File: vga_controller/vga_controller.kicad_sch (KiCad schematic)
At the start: 51 parts

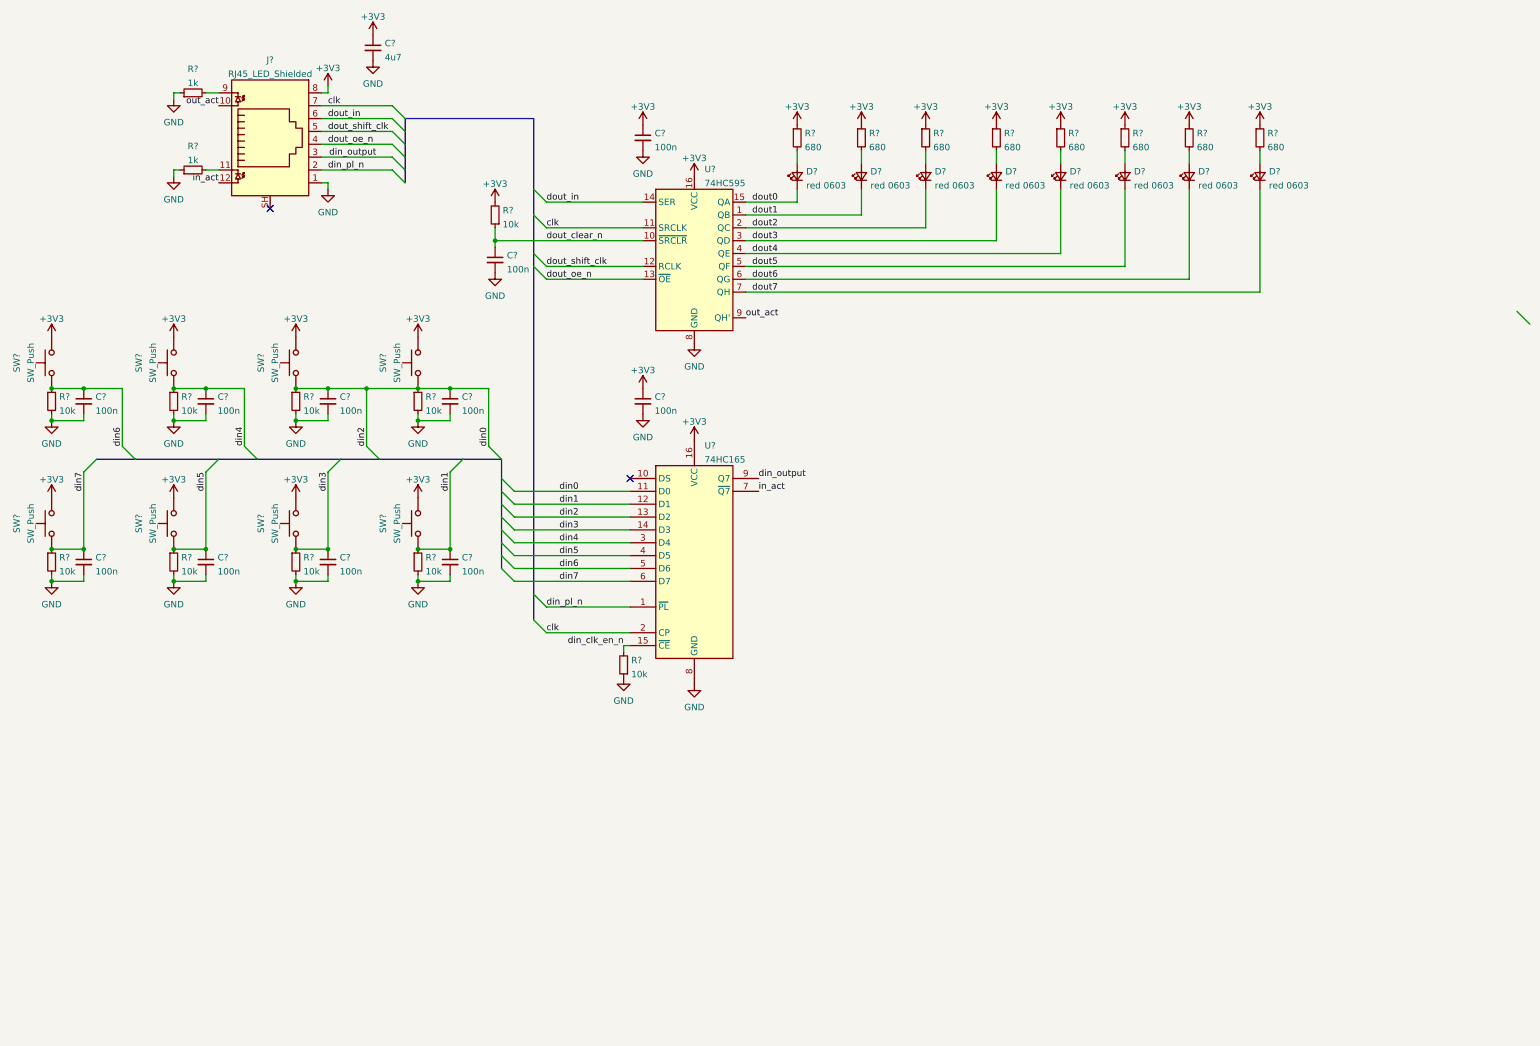
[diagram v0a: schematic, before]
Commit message: schema done, pcb routed
for controller
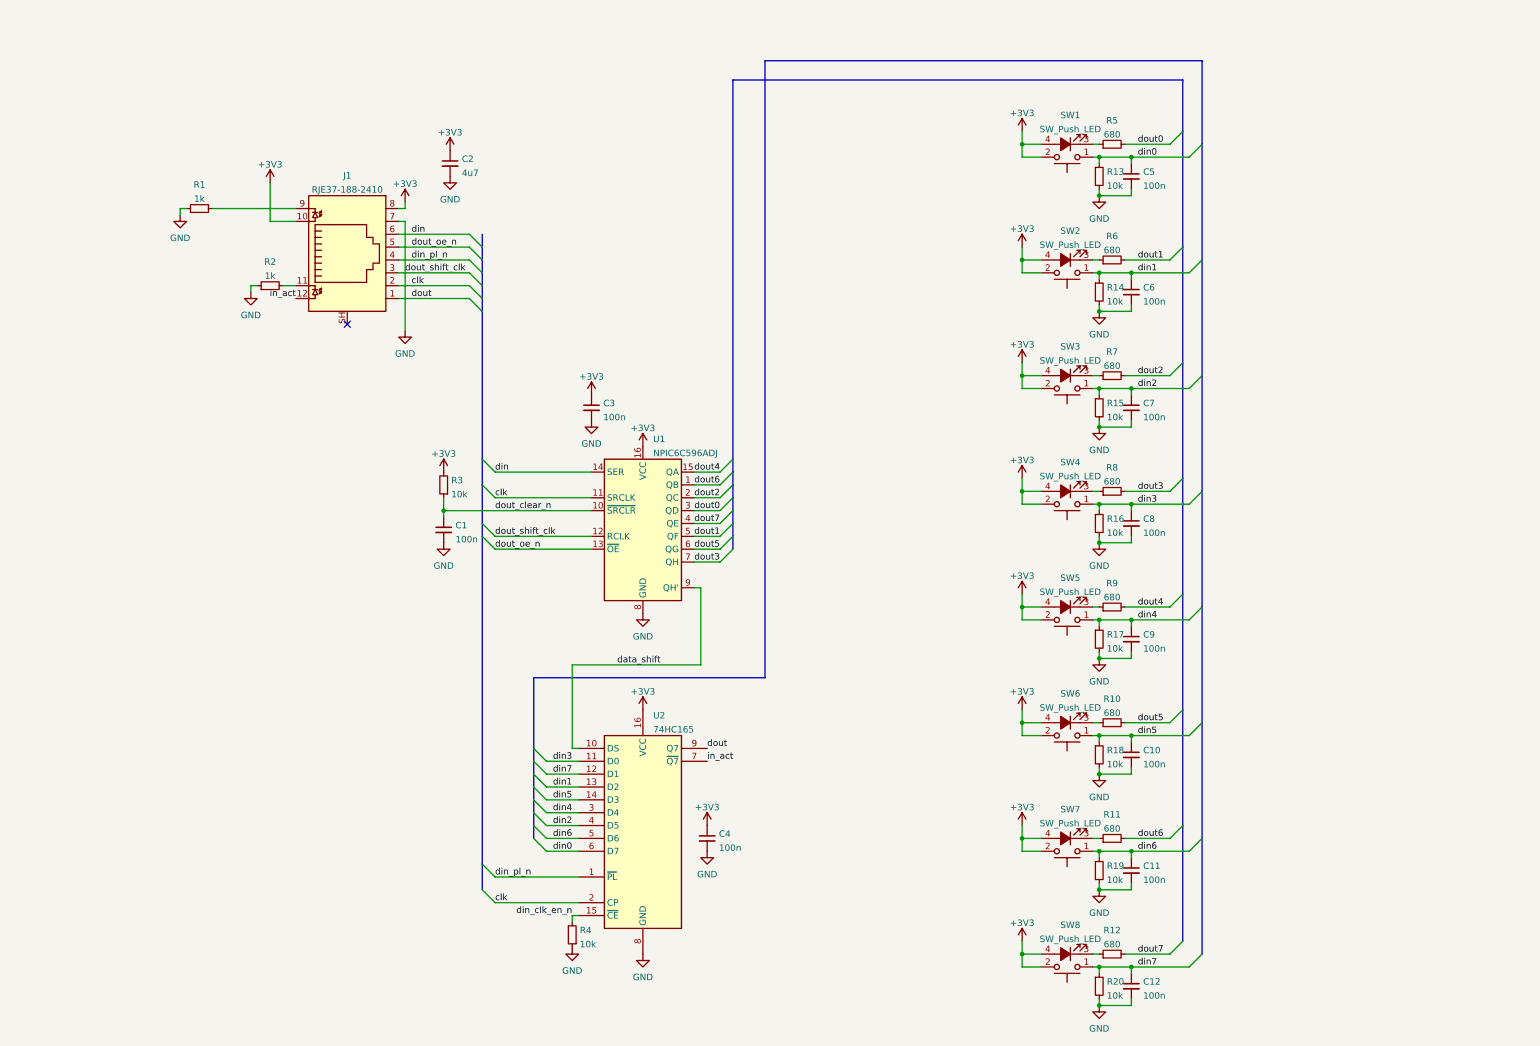
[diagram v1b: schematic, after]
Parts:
- removed C? (x8): 100n, symbol Device:C_Small
- removed D? (x8): red 0603, symbol Device:LED_Small
- removed R? (x8): 680, symbol Device:R_Small
- removed R? (x8): 10k, symbol Device:R_Small
- removed SW? (x8): SW_Push, symbol Switch:SW_Push
- added C10, C11, C12, C5, C6, C7, C8, C9: 100n, Capacitor_SMD:C_0603_1608Metric_Pad1.08x0.95mm_HandSolder, symbol Device:C_Small
- added R10, R11, R12, R5, R6, R7, R8, R9: 680, Resistor_SMD:R_0603_1608Metric_Pad0.98x0.95mm_HandSolder, symbol Device:R_Small
- added R13, R14, R15, R16, R17, R18, R19, R20: 10k, Resistor_SMD:R_0603_1608Metric_Pad0.98x0.95mm_HandSolder, symbol Device:R_Small
- added SW1, SW2, SW3, SW4, SW5, SW6, SW7, SW8: SW_Push_LED, good_things:SW_Cherry_MX_1.00u_PCB_smd_led, symbol Switch:SW_Push_LED
- C1, C2, C3, C4: renamed from C?; footprint (none) -> Capacitor_SMD:C_0603_1608Metric_Pad1.08x0.95mm_HandSolder
- J1: renamed from J?; value RJ45_LED_Shielded -> RJE37-188-2410; footprint (none) -> Connector_RJ:RJ45_Amphenol_RJHSE538X
- R1, R2, R3, R4: renamed from R?; footprint (none) -> Resistor_SMD:R_0603_1608Metric_Pad0.98x0.95mm_HandSolder
- U1: renamed from U?; value 74HC595 -> NPIC6C596ADJ; footprint (none) -> Package_SO:SOIC-16_3.9x9.9mm_P1.27mm
- U2: renamed from U?; footprint (none) -> Package_SO:SOIC-16_3.9x9.9mm_P1.27mm
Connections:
- net +3V3: now also J1.10, SW1.2, SW1.4 (A), SW2.2, SW2.4 (A), SW3.2, SW3.4 (A), SW4.2, SW4.4 (A), SW5.2, SW5.4 (A), SW6.2, SW6.4 (A), SW7.2, SW7.4 (A), SW8.2, SW8.4 (A)
- net GND: now also J1.3, J1.7, U1.12 (RCLK), C10.2, C11.2, C12.2, C5.2, C6.2, C7.2, C8.2, C9.2, R13.2, R14.2, R15.2, R16.2, R17.2, R18.2, R19.2, R20.2; no longer J1.1
- net clk: now also J1.2; no longer J1.7
- net din0: now also U2.6 (D7), C5.1, R13.1, SW1.1; no longer U2.11 (D0), U2.13 (D2)
- net din1: now also U2.13 (D2), C6.1, R14.1, SW2.1; no longer U2.12 (D1)
- net din3: now also U2.11 (D0), C8.1, R16.1, SW4.1; no longer U2.14 (D3)
- net din4: now also C9.1, R17.1, SW5.1
- net din5: now also U2.14 (D3), C10.1, R18.1, SW6.1; no longer U2.4 (D5)
- net din6: now also C11.1, R19.1, SW7.1
- net din7: now also U2.12 (D1), C12.1, R20.1, SW8.1; no longer U2.6 (D7)
- net din_pl_n: now also J1.4; no longer J1.2
- net dout0: now also U1.3 (QD), R5.2; no longer U1.15 (QA)
- net dout1: now also U1.5 (QF), R6.2; no longer U1.1 (QB)
- net dout2: now also R7.2
- net dout3: now also U1.7 (QH), R8.2; no longer U1.3 (QD)
- net dout4: now also U1.15 (QA), R9.2; no longer U1.4 (QE)
- net dout5: now also U1.6 (QG), R10.2; no longer U1.5 (QF)
- net dout6: now also U1.1 (QB), R11.2; no longer U1.6 (QG)
- net dout7: now also U1.4 (QE), R12.2; no longer U1.7 (QH)
- net dout_oe_n: now also J1.5; no longer J1.4
- net data_shift: now reaches U2.10 (DS)
- net data_shift: now also U1.9 (QH')
- net din_output renamed dout
- net dout: now also J1.1; no longer J1.3
- net dout_in renamed din
- removed net dout_shift_clk: J1.5, U1.12 (RCLK)
- removed net out_act: J1.10, U1.9 (QH')
- new net: R10.1, SW6.3 (K)
- new net: R8.1, SW4.3 (K)
- new net: R12.1, SW8.3 (K)
- new net: R9.1, SW5.3 (K)
- new net: R11.1, SW7.3 (K)
- new net: R7.1, SW3.3 (K)
- new net: R5.1, SW1.3 (K)
- new net: R6.1, SW2.3 (K)
- new net din2: C7.1, R15.1, SW3.1, U2.4 (D5)
- no-connect marks 2 -> 1
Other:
- moved on the sheet: C1, C2, C3, C4, J1, R1, R2, R3, R4, U1, U2

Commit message: Rev 4 of main board
controller rev1 done as well :D
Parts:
- added H1, H2, H3: MountingHole_Pad, MountingHole:MountingHole_3.2mm_M3_Pad, symbol Mechanical:MountingHole_Pad
- added R21: 10k, Resistor_SMD:R_0603_1608Metric_Pad0.98x0.95mm_HandSolder, symbol Device:R_Small
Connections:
- net GND: now also J1.5, H1.1, H2.1, H3.1, R21.1; no longer J1.3, U1.12 (RCLK)
- net din renamed copi
- net din_pl_n renamed ie_n
- net dout renamed cipo
- net dout_oe_n renamed oe_n
- net oe_n: now also R21.2; no longer J1.5
- new net out_shift_clk: J1.3, U1.12 (RCLK)
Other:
- moved on the sheet: C10, C11, C12, C5, C6, C7, C8, C9, R10, R11, R12, R13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

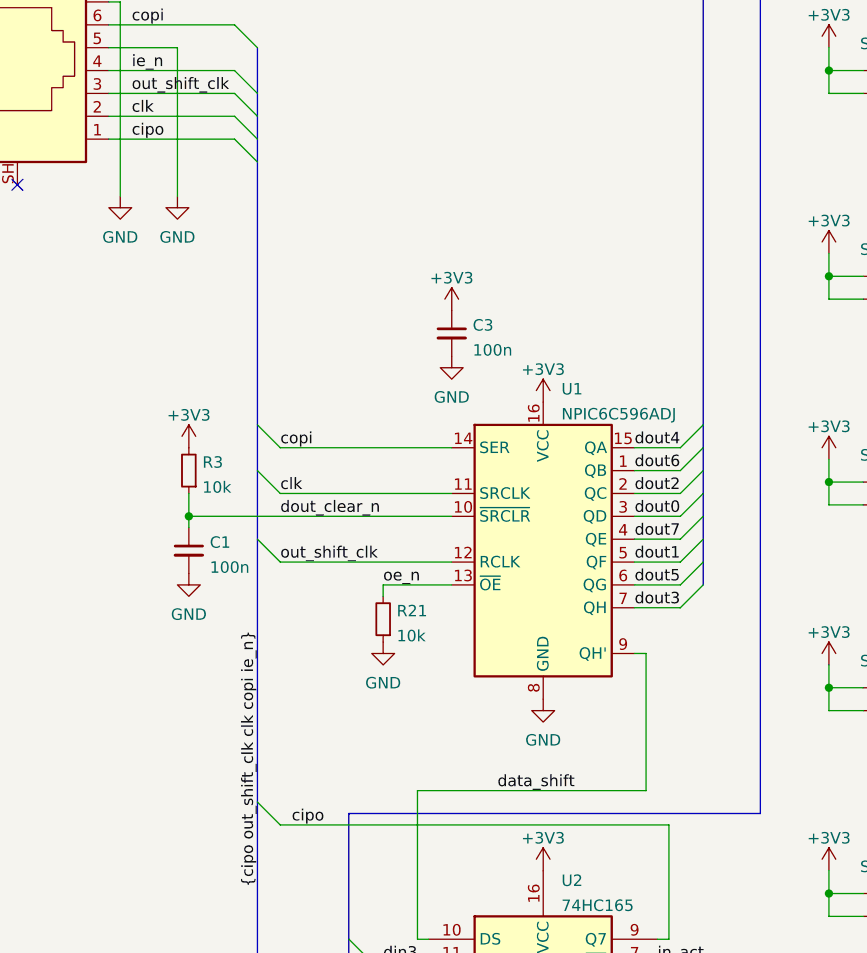
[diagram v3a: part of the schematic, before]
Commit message: fix issue with controller board
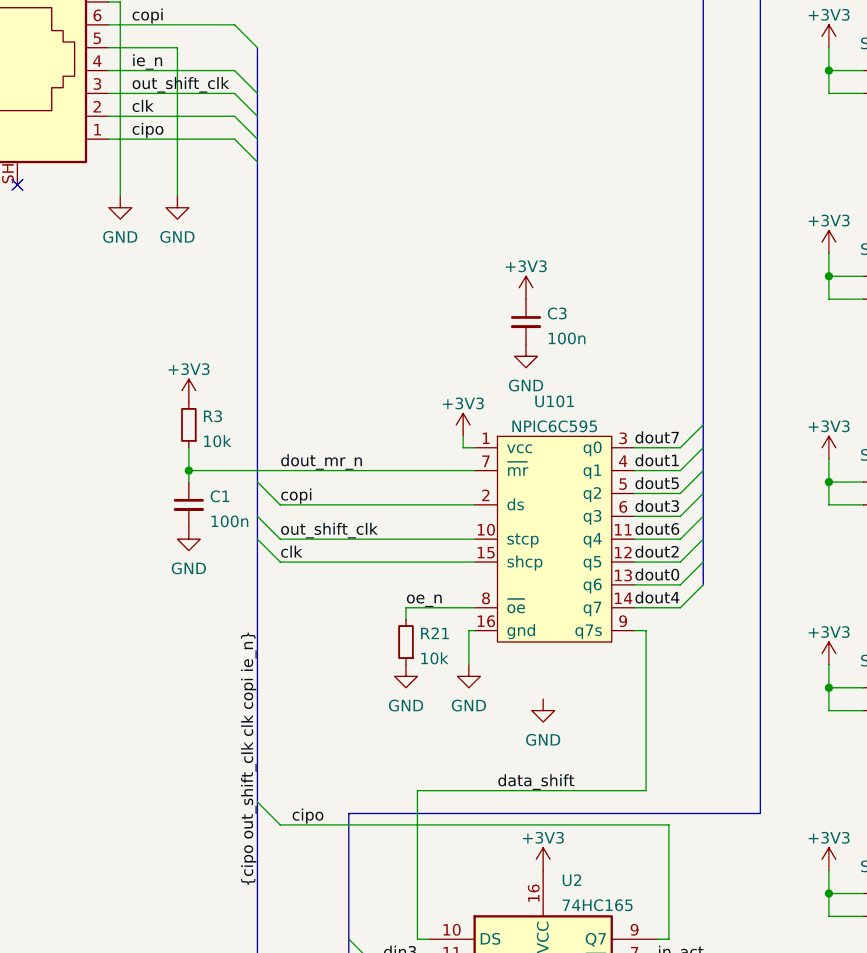
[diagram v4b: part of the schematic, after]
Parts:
- removed U1: NPIC6C596ADJ, Package_SO:SOIC-16_3.9x9.9mm_P1.27mm, symbol 74xx:74HC595
- added U101: NPIC6C595, Package_SO:SOIC-16_3.9x9.9mm_P1.27mm, symbol good_things:NPIC6C595
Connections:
- net +3V3: now also U101.1 (vcc)
- net GND: now also U101.16 (gnd)
- net clk: now also U101.15 (shcp)
- net copi: now also U101.2 (ds)
- net data_shift: now also U101.9 (q7s)
- net dout0: now also U101.13 (q6)
- net dout1: now also U101.4 (q1)
- net dout2: now also U101.12 (q5)
- net dout3: now also U101.6 (q3)
- net dout4: now also U101.14 (q7)
- net dout5: now also U101.5 (q2)
- net dout6: now also U101.11 (q4)
- net dout7: now also U101.3 (q0)
- net oe_n: now also U101.8 (~{oe})
- net out_shift_clk: now also U101.10 (stcp)
- net dout_clear_n renamed dout_mr_n
- net dout_mr_n: now also U101.7 (~{mr})
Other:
- moved on the sheet: C1, C3, R21, R3
